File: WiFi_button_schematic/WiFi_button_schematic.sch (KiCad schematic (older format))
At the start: 13 parts

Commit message: Version v01 finished
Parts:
- added C3: 100nF, Capacitor_SMD:C_0805_2012Metric_Pad1.15x1.40mm_HandSolder, symbol Device:C
- added U3: TC4056A_module, WiFi_button:TC4056_module, symbol WiFi_button:TC4056A_module
- BT1: renamed from BT?; value Battery_Cell -> 3.7V; footprint (none) -> Connector_PinHeader_2.54mm:PinHeader_1x02_P2.54mm_Vertical
- C1, C2: renamed from C?; footprint (none) -> Capacitor_SMD:C_0805_2012Metric_Pad1.15x1.40mm_HandSolder
- D1, D2: renamed from D?; footprint (none) -> LED_SMD:LED_0805_2012Metric_Pad1.15x1.40mm_HandSolder
- J1: renamed from J?; footprint (none) -> Connector_PinHeader_2.54mm:PinHeader_1x05_P2.54mm_Vertical
- R1: renamed from R?; value R -> 47K; footprint (none) -> Resistor_SMD:R_0805_2012Metric_Pad1.15x1.40mm_HandSolder
- R2: renamed from R?; value R -> 10K; footprint (none) -> Resistor_SMD:R_0805_2012Metric_Pad1.15x1.40mm_HandSolder
- R3, R4: renamed from R?; value R -> 1K; footprint (none) -> Resistor_SMD:R_0805_2012Metric_Pad1.15x1.40mm_HandSolder
- SW1: renamed from SW?; footprint (none) -> Button_Switch_THT:SW_PUSH-12mm
- gave numbers to parts that had none: 2
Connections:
- net labels added: Btn
- net labels removed: ~RST
- wire segments 44 -> 64
- no-connect marks 0 -> 1
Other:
- note added: "Decoupling capacitor"
- moved on the sheet: BT1, C1, C2, D1, D2, J1, R1, R2, R3, R4, SW1, U1

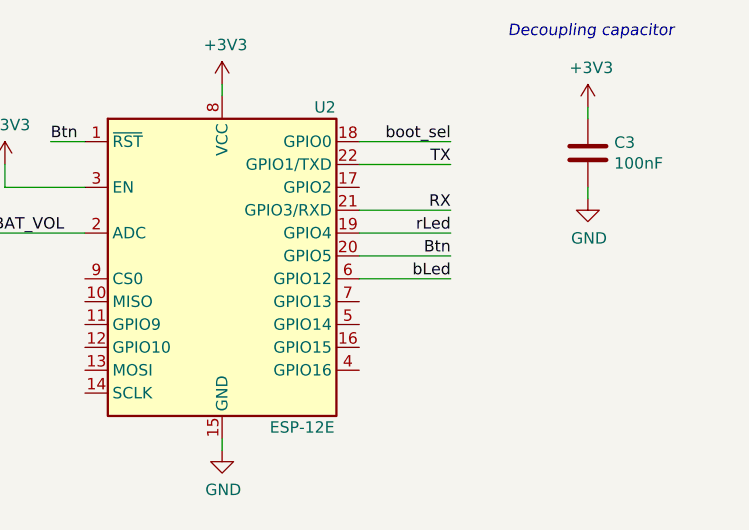
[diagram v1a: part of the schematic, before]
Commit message: Changed capacitors' and resistors' sizes to 1206
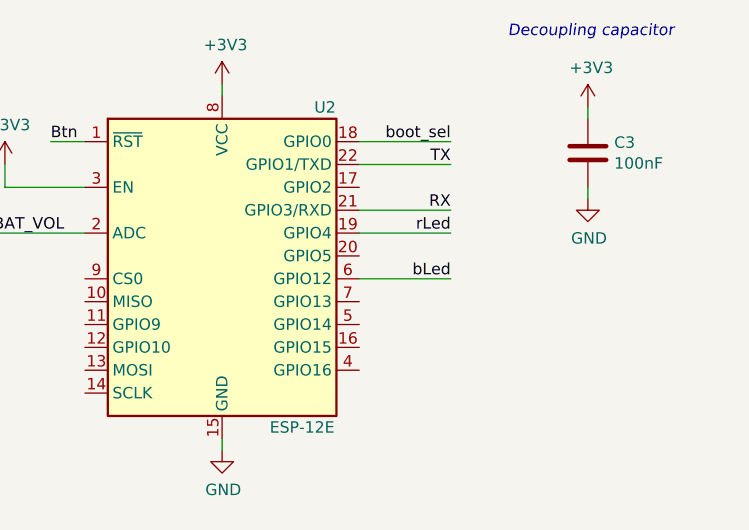
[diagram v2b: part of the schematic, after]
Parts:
- C1, C2, C3: footprint Capacitor_SMD:C_0805_2012Metric_Pad1.15x1.40mm_HandSolder -> Capacitor_SMD:C_1206_3216Metric_Pad1.42x1.75mm_HandSolder
- D1, D2: footprint LED_SMD:LED_0805_2012Metric_Pad1.15x1.40mm_HandSolder -> Capacitor_SMD:C_1206_3216Metric_Pad1.42x1.75mm_HandSolder
- R1, R2, R3, R4: footprint Resistor_SMD:R_0805_2012Metric_Pad1.15x1.40mm_HandSolder -> Capacitor_SMD:C_1206_3216Metric_Pad1.42x1.75mm_HandSolder
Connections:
- wire segments 64 -> 63
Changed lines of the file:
@@
 encoding utf-8
 Sheet 1 1
-Title ""
-Date ""
-Rev ""
+Title "web_button"
+Date "2021-10-04"
+Rev "v02"
 Comp ""
 Comment1 ""
@@
 F 0 "D1" V 3939 1232 50  0000 R CNN
 F 1 "Red" V 3848 1232 50  0000 R CNN
-F 2 "LED_SMD:LED_0805_2012Metric_Pad1.15x1.40mm_HandSolder" H 3900 1350 50  0001 C CNN
+F 2 "Capacitor_SMD:C_1206_3216Metric_Pad1.42x1.75mm_HandSolder" H 3900 1350 50  0001 C CNN
 F 3 "~" H 3900 1350 50  0001 C CNN
 	1    3900 1350
@@
 F 0 "D2" V 4339 1232 50  0000 R CNN
 F 1 "Blue" V 4248 1232 50  0000 R CNN
-F 2 "LED_SMD:LED_0805_2012Metric_Pad1.15x1.40mm_HandSolder" H 4300 1350 50  0001 C CNN
+F 2 "Capacitor_SMD:C_1206_3216Metric_Pad1.42x1.75mm_HandSolder" H 4300 1350 50  0001 C CNN
 F 3 "~" H 4300 1350 50  0001 C CNN
 	1    4300 1350
@@
 F 0 "R3" H 3970 1046 50  0000 L CNN
 F 1 "1K" H 3970 955 50  0000 L CNN
-F 2 "Resistor_SMD:R_0805_2012Metric_Pad1.15x1.40mm_HandSolder" V 3830 1000 50  0001 C CNN
+F 2 "Capacitor_SMD:C_1206_3216Metric_Pad1.42x1.75mm_HandSolder" V 3830 1000 50  0001 C CNN
 F 3 "~" H 3900 1000 50  0001 C CNN
 	1    3900 1000
@@
 F 0 "R4" H 4370 1046 50  0000 L CNN
 F 1 "1K" H 4370 955 50  0000 L CNN
-F 2 "Resistor_SMD:R_0805_2012Metric_Pad1.15x1.40mm_HandSolder" V 4230 1000 50  0001 C CNN
+F 2 "Capacitor_SMD:C_1206_3216Metric_Pad1.42x1.75mm_HandSolder" V 4230 1000 50  0001 C CNN
 F 3 "~" H 4300 1000 50  0001 C CNN
 	1    4300 1000
@@
 F 0 "R1" H 2720 2446 50  0000 L CNN
 F 1 "47K" H 2720 2355 50  0000 L CNN
-F 2 "Resistor_SMD:R_0805_2012Metric_Pad1.15x1.40mm_HandSolder" V 2580 2400 50  0001 C CNN
+F 2 "Capacitor_SMD:C_1206_3216Metric_Pad1.42x1.75mm_HandSolder" V 2580 2400 50  0001 C CNN
 F 3 "~" H 2650 2400 50  0001 C CNN
 	1    2650 2400
@@
 F 0 "R2" H 2720 2846 50  0000 L CNN
 F 1 "10K" H 2720 2755 50  0000 L CNN
-F 2 "Resistor_SMD:R_0805_2012Metric_Pad1.15x1.40mm_HandSolder" V 2580 2800 50  0001 C CNN
+F 2 "Capacitor_SMD:C_1206_3216Metric_Pad1.42x1.75mm_HandSolder" V 2580 2800 50  0001 C CNN
 F 3 "~" H 2650 2800 50  0001 C CNN
 	1    2650 2800
@@
 F 0 "C1" H 1965 1296 50  0000 L CNN
 F 1 "10uF" H 1965 1205 50  0000 L CNN
-F 2 "Capacitor_SMD:C_0805_2012Metric_Pad1.15x1.40mm_HandSolder" H 1888 1100 50  0001 C CNN
+F 2 "Capacitor_SMD:C_1206_3216Metric_Pad1.42x1.75mm_HandSolder" H 1888 1100 50  0001 C CNN
 F 3 "~" H 1850 1250 50  0001 C CNN
 	1    1850 1250
@@
 F 0 "C2" H 3265 1296 50  0000 L CNN
 F 1 "10uF" H 3265 1205 50  0000 L CNN
-F 2 "Capacitor_SMD:C_0805_2012Metric_Pad1.15x1.40mm_HandSolder" H 3188 1100 50  0001 C CNN
+F 2 "Capacitor_SMD:C_1206_3216Metric_Pad1.42x1.75mm_HandSolder" H 3188 1100 50  0001 C CNN
 F 3 "~" H 3150 1250 50  0001 C CNN
 	1    3150 1250
@@
 F 0 "C3" H 7765 1196 50  0000 L CNN
 F 1 "100nF" H 7765 1105 50  0000 L CNN
-F 2 "Capacitor_SMD:C_0805_2012Metric_Pad1.15x1.40mm_HandSolder" H 7688 1000 50  0001 C CNN
+F 2 "Capacitor_SMD:C_1206_3216Metric_Pad1.42x1.75mm_HandSolder" H 7688 1000 50  0001 C CNN
 F 3 "~" H 7650 1150 50  0001 C CNN
 	1    7650 1150
@@
 Text Notes 7300 650  0    50   Italic 0
 Decoupling capacitor
-Text Label 7050 1600 2    50   ~ 0
-Btn
-Wire Wire Line
-	7050 1600 6650 1600
 $EndSCHEMATC

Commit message: Added on-btn and reduced heavily idle current
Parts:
- removed SW1: SW_Push, Button_Switch_THT:SW_PUSH-12mm, symbol Switch:SW_Push
- removed U3: TC4056A_module, WiFi_button:TC4056_module, symbol WiFi_button:TC4056A_module
- added D?: Blue, Capacitor_SMD:C_1206_3216Metric_Pad1.42x1.75mm_HandSolder, symbol Device:LED
- added Q?: 2N3906, Package_TO_SOT_THT:TO-92_Inline, symbol Transistor_BJT:2N3906
- added Q?: 2N3904, Package_TO_SOT_THT:TO-92_Inline, symbol Transistor_BJT:2N3904
- added R?: 4K7, symbol Device:R
- added R?: 10K, symbol Device:R
- added R?: 100K, symbol Device:R
- added R?: 1K, Capacitor_SMD:C_1206_3216Metric_Pad1.42x1.75mm_HandSolder, symbol Device:R
- added SW?: On, symbol Switch:SW_MEC_5G
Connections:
- net labels added: gLed, off_sig
- net labels removed: Btn
- wire segments 63 -> 78
- no-connect marks 1 -> 0
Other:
- note added: "Debug LEDs\n"
- note added: "Main MCU"
- note added: "Power-On switch"
- note added: "Programming Port\n"
- note added: "Voltage Divider"
- note added: "Voltage regulator"
- moved on the sheet: BT1, C1, C2, D1, D2, J1, R1, R2, R3, R4, U1, U2

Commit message: Project is now less complicated
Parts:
- removed J1: Conn_01x05_Male, Connector_PinHeader_2.54mm:PinHeader_1x05_P2.54mm_Vertical, symbol Connector:Conn_01x05_Male
- removed Q?: 2N3906, Package_TO_SOT_THT:TO-92_Inline, symbol Transistor_BJT:2N3906
- removed Q?: 2N3904, Package_TO_SOT_THT:TO-92_Inline, symbol Transistor_BJT:2N3904
- removed R1: 47K, Capacitor_SMD:C_1206_3216Metric_Pad1.42x1.75mm_HandSolder, symbol Device:R
- removed R2: 10K, Capacitor_SMD:C_1206_3216Metric_Pad1.42x1.75mm_HandSolder, symbol Device:R
- removed R?: 4K7, symbol Device:R
- removed R?: 10K, symbol Device:R
- removed R?: 100K, symbol Device:R
- removed SW?: On, symbol Switch:SW_MEC_5G
- added J?: Conn_01x06_Female, symbol Connector:Conn_01x06_Female
- added R? (x3): 10K, symbol Device:R
- added SW? (x2): SW_Push, symbol Switch:SW_Push
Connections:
- net +BATT is gone; now on an unnamed net: C1.1, U1.2 (VIN)
- net +3V3: now also D1.1 (K), D2.1 (K), D?.1 (K), J?.3 (Pin_3), R?.1, R?.1, SW?.2; no longer U2.1 (~RST)
- net GND: now also J?.1 (Pin_1), R?.1, SW?.1; no longer D1.1 (K), D2.1 (K), D?.1 (K)
- net RX: now also J?.4 (Pin_4)
- net TX: now also J?.5 (Pin_5)
- net boot_sel: now also R?.2, SW?.1
- net off_sig: no longer names the net of U2.17 (GPIO2)
- net off_sig: now also R?.2
- new net ~RST: R?.2, SW?.2, U2.1 (~RST)
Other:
- note added: "CTS"
- note added: "DTR"
- note added: "FLASH"
- note added: "RST"
- note added: "VCC"
- note removed: "3V3\n"
- note removed: "Power-On switch"
- note removed: "Voltage Divider"
- note removed: "boot\n"
- moved on the sheet: BT1, C1, C2, C3, D1, D2, D?, R3, R4, R?, U1

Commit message: V02 of schematic finished
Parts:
- removed R?: 10K, symbol Device:R
- removed SW?: SW_Push, symbol Switch:SW_Push
- added Q1, Q2: MMBT3904, Package_TO_SOT_SMD:SOT-23_Handsoldering, symbol Transistor_BJT:MMBT3904
- added R1, R3: 10K, Resistor_SMD:R_1206_3216Metric_Pad1.30x1.75mm_HandSolder, symbol Device:R
- C1, C2, C3: footprint Capacitor_SMD:C_1206_3216Metric_Pad1.42x1.75mm_HandSolder -> Capacitor_SMD:C_1206_3216Metric_Pad1.33x1.80mm_HandSolder
- D1: footprint Capacitor_SMD:C_1206_3216Metric_Pad1.42x1.75mm_HandSolder -> LED_SMD:LED_1206_3216Metric_Pad1.42x1.75mm_HandSolder
- D2: value Blue -> Green; footprint Capacitor_SMD:C_1206_3216Metric_Pad1.42x1.75mm_HandSolder -> LED_SMD:LED_1206_3216Metric_Pad1.42x1.75mm_HandSolder
- D3: renamed from D?; value Blue -> Green; footprint Capacitor_SMD:C_1206_3216Metric_Pad1.42x1.75mm_HandSolder -> LED_SMD:LED_1206_3216Metric_Pad1.42x1.75mm_HandSolder
- J1: renamed from J?; footprint (none) -> Connector_PinHeader_2.54mm:PinHeader_1x06_P2.54mm_Vertical
- R2: renamed from R3; footprint Capacitor_SMD:C_1206_3216Metric_Pad1.42x1.75mm_HandSolder -> Resistor_SMD:R_1206_3216Metric_Pad1.30x1.75mm_HandSolder
- R4: footprint Capacitor_SMD:C_1206_3216Metric_Pad1.42x1.75mm_HandSolder -> Resistor_SMD:R_1206_3216Metric_Pad1.30x1.75mm_HandSolder
- R5: renamed from R?; footprint Capacitor_SMD:C_1206_3216Metric_Pad1.42x1.75mm_HandSolder -> Resistor_SMD:R_1206_3216Metric_Pad1.30x1.75mm_HandSolder
- R8, R9: renamed from R?; footprint (none) -> Resistor_SMD:R_1206_3216Metric_Pad1.30x1.75mm_HandSolder
- SW1: renamed from SW?; footprint (none) -> custom_buttons_switches:sw_push_12_x_12_mm
- U1: footprint Package_TO_SOT_SMD:SOT-89-3 -> Package_TO_SOT_SMD:SOT-89-3_Handsoldering
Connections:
- net +3V3: no longer R9.1
- net GND: now also R9.2
- net bLed: now also U2.20 (GPIO5); no longer U2.6 (GPIO12)
- net boot_sel: now also Q2.3 (C)
- net gLed: now also U2.6 (GPIO12); no longer U2.20 (GPIO5)
- net ~RST: now also Q1.3 (C)
- net at U2.16 (GPIO15): now also R9.1
- net at U2.17 (GPIO2): no longer R9.2
- net +BATT: now reaches BT1.1 (+), C1.1, U1.2 (VIN)
- net CTS: now reaches J1.2 (Pin_2)
- net CTS: now also Q1.2 (E), R3.1
- net DTR: now reaches J1.6 (Pin_6)
- net DTR: now also Q2.2 (E), R1.1
- net BAT_VOL: no longer names the net of U2.2 (ADC)
- new net: Q1.1 (B), R1.2
- new net: Q2.1 (B), R3.2
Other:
- note added: "3 AAA alkaine batteries in series"
- note removed: "FLASH"
- moved on the sheet: R8, R9, SW1

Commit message: Added circuit for measuring battery voltage
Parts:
- added Q3: MMBT3904, Package_TO_SOT_SMD:SOT-23_Handsoldering, symbol Transistor_BJT:MMBT3904
- added Q4: MMBT3906, Package_TO_SOT_SMD:SOT-23_Handsoldering, symbol Transistor_BJT:MMBT3906
- added R10: 10K, Resistor_SMD:R_1206_3216Metric_Pad1.30x1.75mm_HandSolder, symbol Device:R
- added R6, R7: 47K, Resistor_SMD:R_1206_3216Metric_Pad1.30x1.75mm_HandSolder, symbol Device:R
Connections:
- net +BATT: now also Q4.3 (C)
- net GND: now also Q3.2 (E), R10.2
- net ADC_IN: now reaches U2.2 (ADC)
- net ADC_IN: now also R10.1, R7.2
- net ADC_EN: now reaches U2.7 (GPIO13)
- net ADC_EN: now also R6.2
- new net: Q3.3 (C), Q4.1 (B)
- new net: Q4.2 (E), R7.1
- new net: Q3.1 (B), R6.1
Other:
- note added: "Auto-reset and auto-boot"
- note added: "Measure battery voltage"
- note added: "Voltage regulator 2.5V"
- note removed: "Voltage regulator"
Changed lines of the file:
@@
 Wire Wire Line
 	1450 1750 2150 1750
-Text Notes 1850 950  0    50   Italic 0
-Voltage regulator
+Text Notes 1750 950  0    50   Italic 0
+Voltage regulator 2.5V
 Text Notes 850  3150 0    50   Italic 0
 Programming Port\n
@@
 Wire Wire Line
 	2300 6050 2300 6150
+$Comp
+L power:+BATT #PWR0102
+U 1 1 61A81EC9
+P 4800 5600
+F 0 "#PWR0102" H 4800 5450 50  0001 C CNN
+F 1 "+BATT" H 4815 5773 50  0000 C CNN
+F 2 "" H 4800 5600 50  0001 C CNN
+F 3 "" H 4800 5600 50  0001 C CNN
+	1    4800 5600
+	1    0    0    -1
+$EndComp
+$Comp
+L Transistor_BJT:MMBT3906 Q4
+U 1 1 61A825D7
+P 4700 5850
+F 0 "Q4" H 4891 5896 50  0000 L CNN
+F 1 "MMBT3906" H 4891 5805 50  0000 L CNN
+F 2 "Package_TO_SOT_SMD:SOT-23_Handsoldering" H 4900 5775 50  0001 L CIN
+F 3 "https://www.onsemi.com/pub/Collateral/2N3906-D.PDF" H 4700 5850 50  0001 L CNN
+	1    4700 5850
+	1    0    0    -1
+$EndComp
+$Comp
+L Transistor_BJT:MMBT3904 Q3
+U 1 1 61A85704
+P 4300 6150
+F 0 "Q3" V 4500 6100 50  0000 L CNN
+F 1 "MMBT3904" V 4600 5950 50  0000 L CNN
+F 2 "Package_TO_SOT_SMD:SOT-23_Handsoldering" H 4500 6075 50  0001 L CIN
+F 3 "https://www.onsemi.com/pub/Collateral/2N3903-D.PDF" H 4300 6150 50  0001 L CNN
+	1    4300 6150
+	1    0    0    -1
+$EndComp
+Wire Wire Line
+	4400 5950 4400 5850
+Wire Wire Line
+	4400 5850 4500 5850
+Wire Wire Line
+	4800 5650 4800 5600
+$Comp
+L Device:R R7
+U 1 1 61A8AAFD
+P 4800 6250
+F 0 "R7" H 4870 6296 50  0000 L CNN
+F 1 "47K" H 4870 6205 50  0000 L CNN
+F 2 "Resistor_SMD:R_1206_3216Metric_Pad1.30x1.75mm_HandSolder" V 4730 6250 50  0001 C CNN
+F 3 "~" H 4800 6250 50  0001 C CNN
+	1    4800 6250
+	1    0    0    -1
+$EndComp
+Wire Wire Line
+	4800 6100 4800 6050
+$Comp
+L Device:R R10
+U 1 1 61A8D04D
+P 4800 6650
+F 0 "R10" H 4870 6696 50  0000 L CNN
+F 1 "10K" H 4870 6605 50  0000 L CNN
+F 2 "Resistor_SMD:R_1206_3216Metric_Pad1.30x1.75mm_HandSolder" V 4730 6650 50  0001 C CNN
+F 3 "~" H 4800 6650 50  0001 C CNN
+	1    4800 6650
+	1    0    0    -1
+$EndComp
+Wire Wire Line
+	4800 6500 4800 6450
+Text Label 5150 6450 2    50   ~ 0
+ADC_IN
+Wire Wire Line
+	5150 6450 4800 6450
+Connection ~ 4800 6450
+Wire Wire Line
+	4800 6450 4800 6400
+$Comp
+L power:GND #PWR0103
+U 1 1 61A91483
+P 4800 6850
+F 0 "#PWR0103" H 4800 6600 50  0001 C CNN
+F 1 "GND" H 4805 6677 50  0000 C CNN
+F 2 "" H 4800 6850 50  0001 C CNN
+F 3 "" H 4800 6850 50  0001 C CNN
+	1    4800 6850
+	1    0    0    -1
+$EndComp
+Wire Wire Line
+	4800 6850 4800 6800
+$Comp
+L power:GND #PWR0104
+U 1 1 61A9386F
+P 4400 6400
+F 0 "#PWR0104" H 4400 6150 50  0001 C CNN
+F 1 "GND" H 4405 6227 50  0000 C CNN
+F 2 "" H 4400 6400 50  0001 C CNN
+F 3 "" H 4400 6400 50  0001 C CNN
+	1    4400 6400
+	1    0    0    -1
+$EndComp
+Wire Wire Line
+	4400 6400 4400 6350
+$Comp
+L Device:R R6
+U 1 1 61A976CE
+P 3900 6150
+F 0 "R6" V 3693 6150 50  0000 C CNN
+F 1 "47K" V 3784 6150 50  0000 C CNN
+F 2 "Resistor_SMD:R_1206_3216Metric_Pad1.30x1.75mm_HandSolder" V 3830 6150 50  0001 C CNN
+F 3 "~" H 3900 6150 50  0001 C CNN
+	1    3900 6150
+	0    1    1    0
+$EndComp
+Wire Wire Line
+	4050 6150 4100 6150
+Text Label 3450 6150 0    50   ~ 0
+ADC_EN
+Wire Wire Line
+	3450 6150 3750 6150
+Text Notes 1400 4550 0    50   ~ 0
+Auto-reset and auto-boot
+Text Notes 4400 5350 0    50   ~ 0
+Measure battery voltage
+Text Label 4950 2300 0    50   ~ 0
+ADC_IN
+Wire Wire Line
+	4950 2300 5300 2300
+Text Label 6900 2600 2    50   ~ 0
+ADC_EN
+Wire Wire Line
+	6500 2600 6900 2600
 $EndSCHEMATC

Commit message: Version v02
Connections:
- net +BATT: now also Q4.2 (E); no longer Q4.3 (C)
- net at R7.1: now also Q4.3 (C); no longer Q4.2 (E)
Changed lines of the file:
@@
 F 3 "https://www.onsemi.com/pub/Collateral/2N3906-D.PDF" H 4700 5850 50  0001 L CNN
 	1    4700 5850
-	1    0    0    -1
+	1    0    0    1
 $EndComp
 $Comp
